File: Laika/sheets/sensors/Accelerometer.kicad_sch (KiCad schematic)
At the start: 0 parts

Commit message: Created schematic for ADXL373 Accelerometer
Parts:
- added C21, C22: 0.1u, symbol Device:C
- added U9: ADXL373, Sensor_Motion:Analog_LGA-16_3.25x3mm_P0.5mm_LayoutBorder3x5y, symbol LaikaSensors:ADXL373
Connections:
- new net +3V3: C21.1, C22.1, U9.1 (V_{DD_I/O}), U9.14 (V_{S})
- new net ACCEL_CS: U9.8 (~{CS})
- new net ACCEL_INT: U9.11 (INT1)
- new net ACCEL_SCLK: U9.4 (SCLK)
- new net ACCEL_SDI: U9.6 (MOSI)
- new net ACCEL_SDO: U9.7 (MISO)
- new net GND: C21.2, C22.2, U9.12 (GND), U9.13 (GND), U9.16 (GND)
- no-connect marks 0 -> 4
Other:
- note added: "Accelerometer"

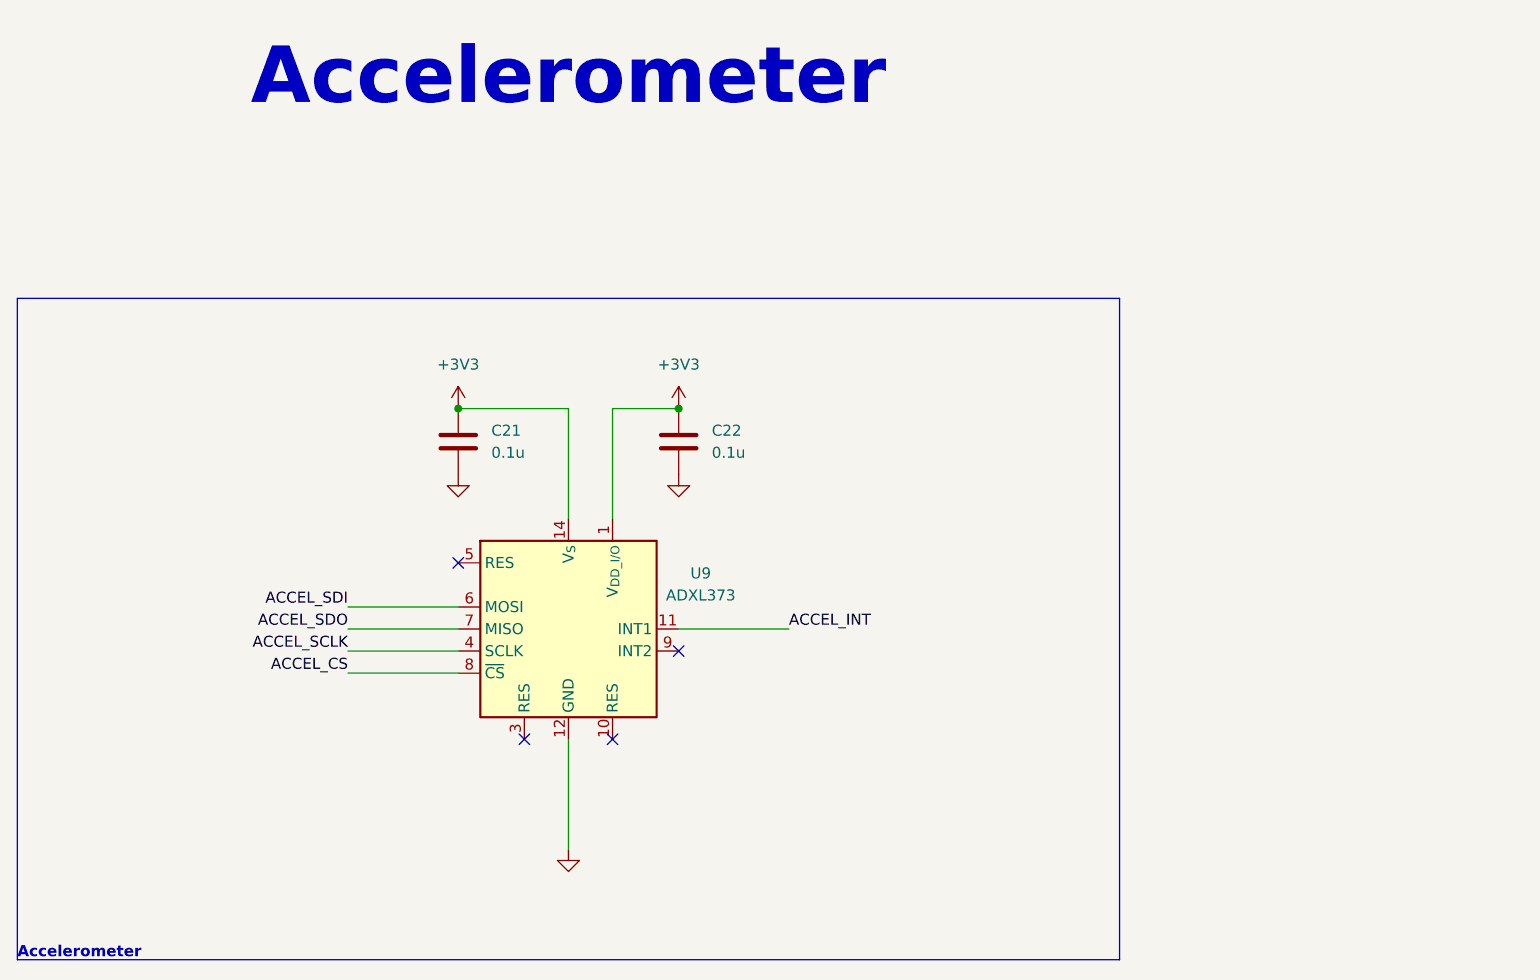
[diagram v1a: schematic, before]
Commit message: Connected sensors to SPI3
Connected Sensor Bus to SPI3. Rearranged GPS reset, pps, and buzzer pins
to other 3.3V logic pins. Connected SPI chip selects. Deleted interrupt
bus from sensors due to lack of 3.3V pins.
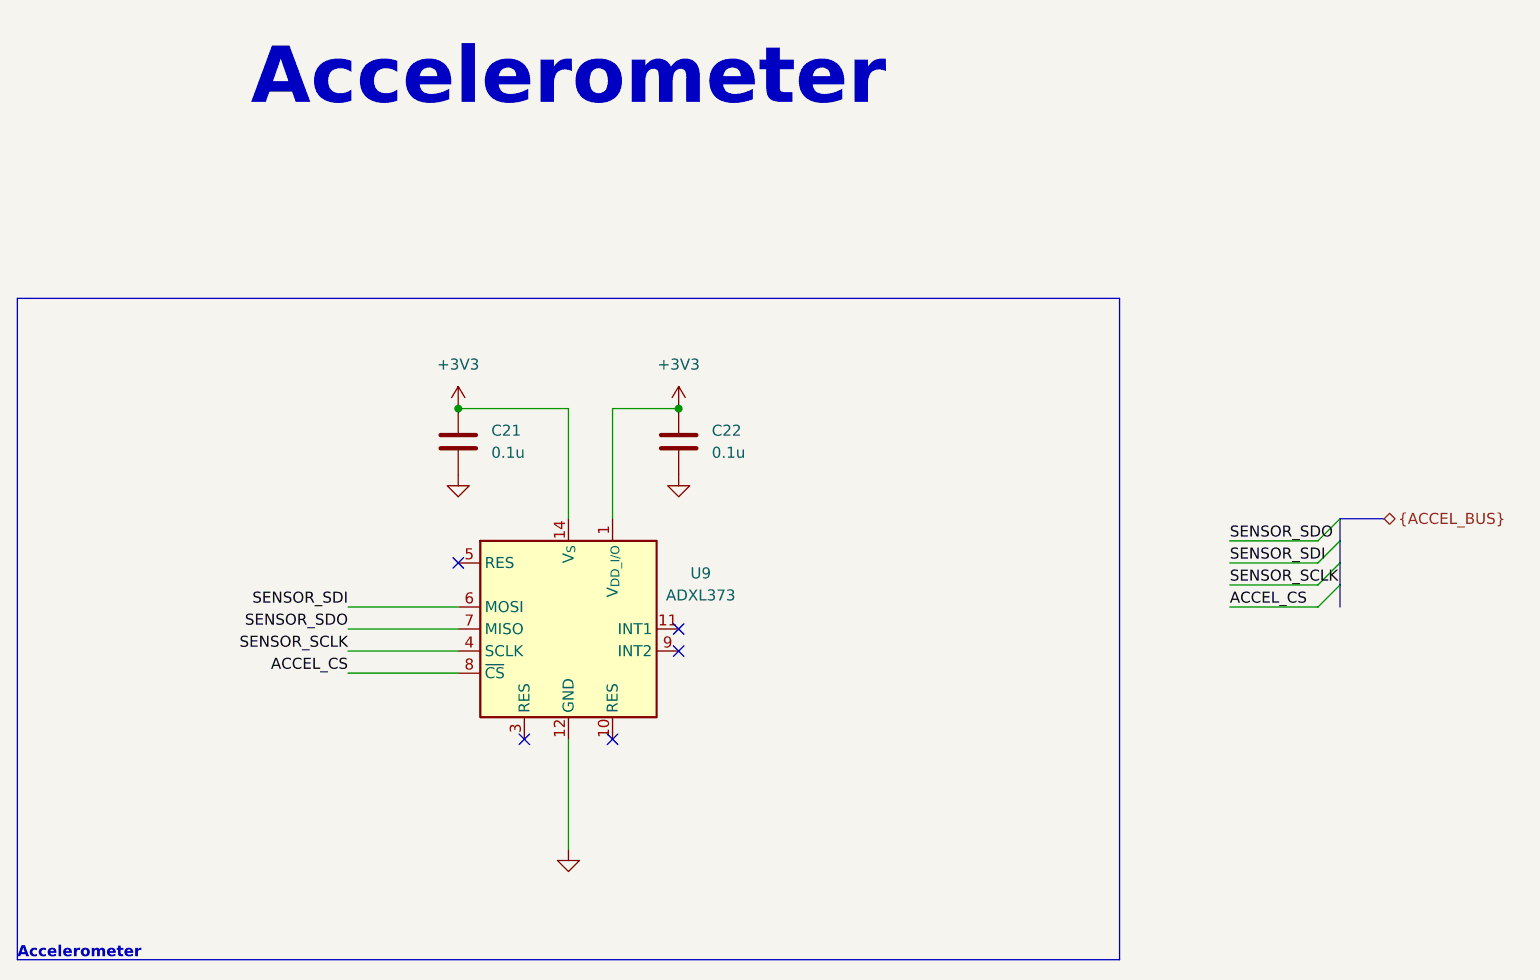
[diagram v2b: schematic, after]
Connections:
- net ACCEL_INT: no longer names the net of U9.11 (INT1)
- net ACCEL_SCLK renamed SENSOR_SCLK
- net ACCEL_SDI renamed SENSOR_SDI
- net ACCEL_SDO renamed SENSOR_SDO
- no-connect marks 4 -> 5
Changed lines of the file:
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@@
 		(comment 1 "${VARIANT}")
+	)
+	(bus_alias "ACCEL_BUS"
+		(members "SENSOR_SDO" "SENSOR_SDI" "SENSOR_SCLK" "ACCEL_CS")
 	)
 	(rectangle
@@
 	)
 	(no_connect
+		(at 152.4 88.9)
+	)
+	(no_connect
 		(at 152.4 91.44)
 	)
@@
 		(at 134.62 101.6)
 	)
+	(bus_entry
+		(at 228.6 81.28)
+		(size -2.54 2.54)
+		(stroke
+			(width 0)
+			(type default)
+		)
+	)
+	(bus_entry
+		(at 228.6 78.74)
+		(size -2.54 2.54)
+		(stroke
+			(width 0)
+			(type default)
+		)
+	)
+	(bus_entry
+		(at 228.6 83.82)
+		(size -2.54 2.54)
+		(stroke
+			(width 0)
+			(type default)
+		)
+	)
+	(bus_entry
+		(at 228.6 76.2)
+		(size -2.54 2.54)
+		(stroke
+			(width 0)
+			(type default)
+		)
+	)
+	(bus
+		(pts
+			(xy 228.6 81.28) (xy 228.6 83.82)
+		)
+		(stroke
+			(width 0)
+			(type default)
+		)
+	)
+	(wire
+		(pts
+			(xy 215.9 86.36) (xy 226.06 86.36)
+		)
+		(stroke
+			(width 0)
+			(type default)
+		)
+	)
 	(wire
 		(pts
@@
 	(wire
 		(pts
-			(xy 165.1 88.9) (xy 152.4 88.9)
+			(xy 215.9 81.28) (xy 226.06 81.28)
+		)
+		(stroke
+			(width 0)
+			(type default)
+		)
+	)
+	(bus
+		(pts
+			(xy 228.6 78.74) (xy 228.6 81.28)
 		)
 		(stroke
@@
 		)
 	)
+	(bus
+		(pts
+			(xy 233.68 76.2) (xy 228.6 76.2)
+		)
+		(stroke
+			(width 0)
+			(type default)
+		)
+	)
+	(bus
+		(pts
+			(xy 228.6 83.82) (xy 228.6 86.36)
+		)
+		(stroke
+			(width 0)
+			(type default)
+		)
+	)
+	(bus
+		(pts
+			(xy 228.6 76.2) (xy 228.6 78.74)
+		)
+		(stroke
+			(width 0)
+			(type default)
+		)
+	)
 	(wire
 		(pts
@@
 	(wire
 		(pts
+			(xy 215.9 78.74) (xy 226.06 78.74)
+		)
+		(stroke
+			(width 0)
+			(type default)
+		)
+	)
+	(wire
+		(pts
 			(xy 139.7 63.5) (xy 127 63.5)
 		)
@@
 	(wire
 		(pts
+			(xy 215.9 83.82) (xy 226.06 83.82)
+		)
+		(stroke
+			(width 0)
+			(type default)
+		)
+	)
+	(wire
+		(pts
 			(xy 114.3 86.36) (xy 127 86.36)
 		)
@@
 		)
 	)
-	(label "ACCEL_SCLK"
+	(label "ACCEL_CS"
+		(at 215.9 86.36 0)
+		(effects
+			(font
+				(size 1.27 1.27)
+			)
+			(justify left bottom)
+		)
+	)
+	(label "SENSOR_SDO"
+		(at 215.9 78.74 0)
+		(effects
+			(font
+				(size 1.27 1.27)
+			)
+			(justify left bottom)
+		)
+	)
+	(label "SENSOR_SCLK"
 		(at 114.3 91.44 180)
 		(effects
@@
 		)
 	)
-	(label "ACCEL_SDI"
+	(label "SENSOR_SDI"
 		(at 114.3 86.36 180)
 		(effects
@@
 		)
 	)
-	(label "ACCEL_INT"
-		(at 165.1 88.9 0)
-		(effects
-			(font
-				(size 1.27 1.27)
-			)
-			(justify left bottom)
-		)
-	)
-	(label "ACCEL_SDO"
+	(label "SENSOR_SDI"
+		(at 215.9 81.28 0)
+		(effects
+			(font
+				(size 1.27 1.27)
+			)
+			(justify left bottom)
+		)
+	)
+	(label "SENSOR_SDO"
 		(at 114.3 88.9 180)
 		(effects
@@
 		)
 	)
+	(label "SENSOR_SCLK"
+		(at 215.9 83.82 0)
+		(effects
+			(font
+				(size 1.27 1.27)
+			)
+			(justify left bottom)
+		)
+	)
+	(hierarchical_label "{ACCEL_BUS}"
+		(shape bidirectional)
+		(at 233.68 76.2 0)
+		(effects
+			(font
+				(size 1.27 1.27)
+			)
+			(justify left)
+		)
+	)

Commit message: Populated BOM with part numbers and footprints
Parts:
- C21, C22: footprint (none) -> Capacitor_SMD:C_0402_1005Metric; JLC Part Type (none) -> Basic; Manafacturer (none) -> Samsung Electro-Mechanics; Part Number (none) -> CL05B104KO5NNNC
- U9: JLC Part Type (none) -> Extended; Manafacturer (none) -> Analog Devices Inc.; Part Number (none) -> ADXL373BCCZ-RL7
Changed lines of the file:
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@@
+			)
+		)
+		(property "JLC Part Type" "Extended"
+			(at 139.7 88.9 0)
+			(effects
+				(font
+					(size 1.27 1.27)
+				)
+				(hide yes)
+			)
+		)
+		(property "Manafacturer" "Analog Devices Inc."
+			(at 139.7 88.9 0)
+			(effects
+				(font
+					(size 1.27 1.27)
+				)
+				(hide yes)
+			)
+		)
+		(property "Part Number" "ADXL373BCCZ-RL7 "
+			(at 139.7 88.9 0)
+			(effects
+				(font
+					(size 1.27 1.27)
+				)
+				(hide yes)
 			)
 		)
@@
 			)
 		)
-		(property "Footprint" ""
+		(property "Footprint" "Capacitor_SMD:C_0402_1005Metric"
 			(at 127.9652 71.12 0)
 			(effects
@@
 			)
 		)
-		(property "Datasheet" "~"
+		(property "Datasheet" "https://www.samsungsem.com/resources/file/global/support/product_catalog/MLCC.pdf"
 			(at 127 67.31 0)
 			(effects
@@
 		)
 		(property "Description" "Unpolarized capacitor"
+			(at 127 67.31 0)
+			(effects
+				(font
+					(size 1.27 1.27)
+				)
+				(hide yes)
+			)
+		)
+		(property "JLC Part Type" "Basic"
+			(at 127 67.31 0)
+			(effects
+				(font
+					(size 1.27 1.27)
+				)
+				(hide yes)
+			)
+		)
+		(property "Manafacturer" "Samsung Electro-Mechanics"
+			(at 127 67.31 0)
+			(effects
+				(font
+					(size 1.27 1.27)
+				)
+				(hide yes)
+			)
+		)
+		(property "Part Number" "CL05B104KO5NNNC"
 			(at 127 67.31 0)
 			(effects
@@
 			)
 		)
-		(property "Footprint" ""
+		(property "Footprint" "Capacitor_SMD:C_0402_1005Metric"
 			(at 153.3652 71.12 0)
 			(effects
@@
 			)
 		)
-		(property "Datasheet" "~"
+		(property "Datasheet" "https://www.samsungsem.com/resources/file/global/support/product_catalog/MLCC.pdf"
 			(at 152.4 67.31 0)
 			(effects
@@
 			(at 152.4 67.31 0)
 			(effects
+				(font
+					(size 1.27 1.27)
+				)
+				(hide yes)
+			)
+		)
+		(property "JLC Part Type" "Basic"
+			(at 152.4 67.31 0)
+			(effects
+				(font
+					(size 1.27 1.27)
+				)
+				(hide yes)
+			)
+		)
+		(property "Manafacturer" "Samsung Electro-Mechanics"
+			(at 152.4 67.31 0)
+			(effects
+				(font
+					(size 1.27 1.27)
+				)
+				(hide yes)
+			)
+		)
+		(property "Part Number" "CL05B104KO5NNNC"
+			(at 152.4 67.31 0)
+			(effects
